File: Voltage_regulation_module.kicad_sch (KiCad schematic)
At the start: 10 parts, among them J5 PJ-202A, U6 L7805CV, U7 LD1117V33

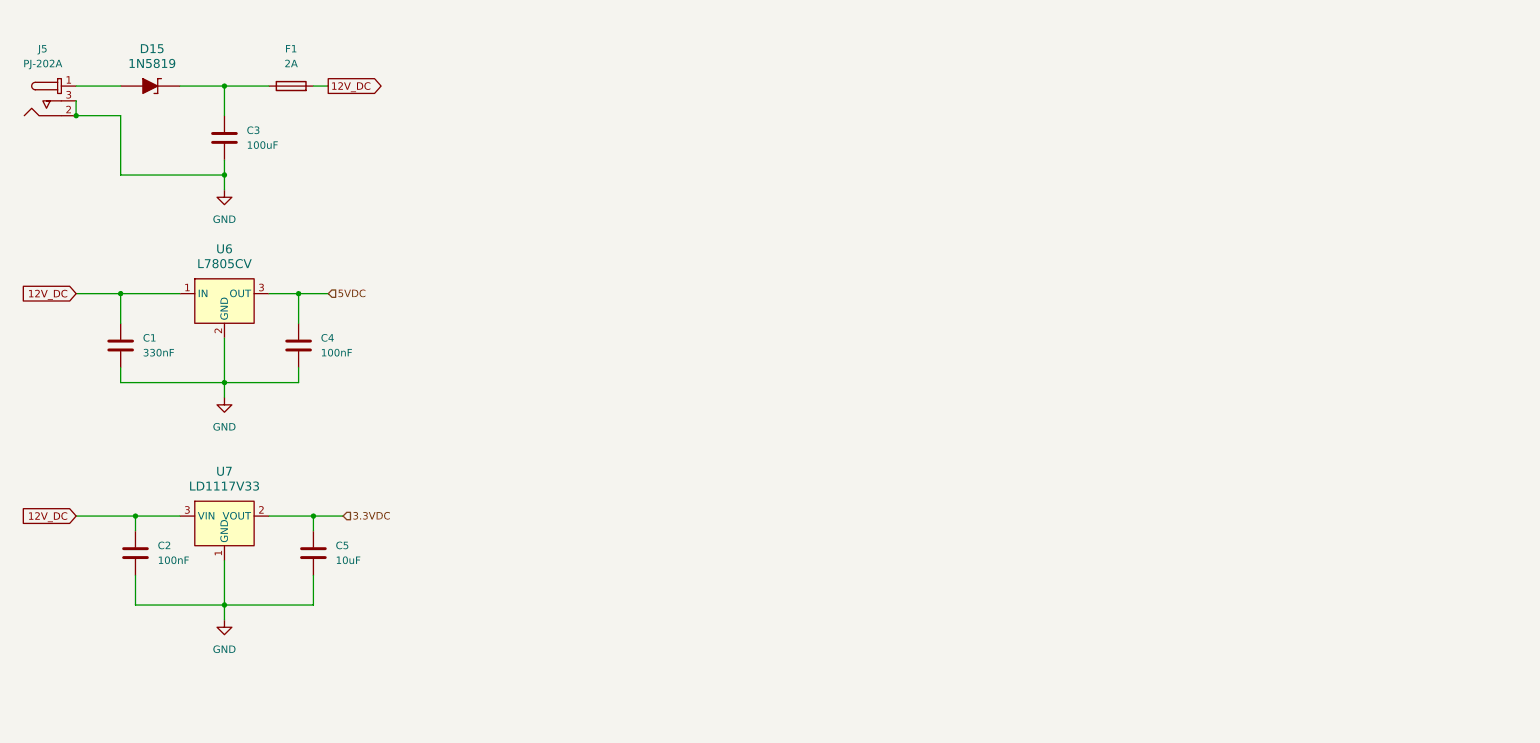
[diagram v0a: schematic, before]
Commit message: PCB REV 001 design
The design of the first revition of the PCB is complete.
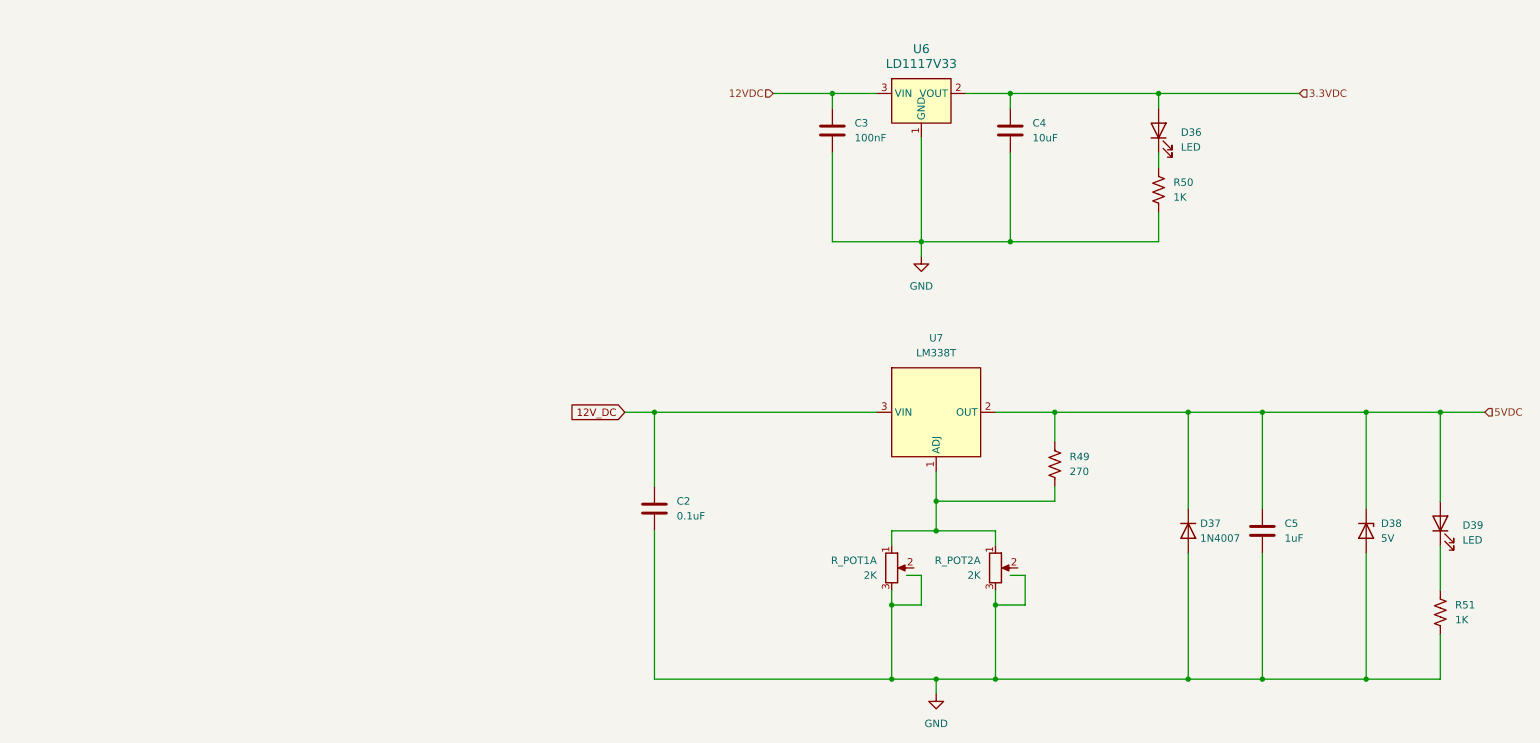
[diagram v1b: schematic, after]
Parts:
- removed C3: 100uF, Capacitor_THT:CP_Radial_D8.0mm_P5.00mm, symbol Device:C
- removed C4: 100nF, Capacitor_THT:C_Disc_D8.0mm_W5.0mm_P5.00mm, symbol Device:C
- removed D15: 1N5819, digikey-footprints:DO-41, symbol dk_Diodes-Rectifiers-Single:1N5819
- removed F1: 2A, Fuse:Fuseholder_Clip-5x20mm_Bel_FC-203-22_Lateral_P17.80x5.00mm_D1.17mm_Horizontal, symbol Device:Fuse
- removed J5: PJ-202A, digikey-footprints:Barrel_Jack_5.5mmODx2.1mmID_PJ-202A, symbol dk_Barrel-Power-Connectors:PJ-202A
- removed U6: L7805CV, digikey-footprints:TO-220-3, symbol dk_PMIC-Voltage-Regulators-Linear:L7805CV
- added C5: 1uF, Capacitor_THT:C_Radial_D10.0mm_H12.5mm_P5.00mm, symbol Device:C
- added D36, D39: LED, LED_THT:LED_D3.0mm, symbol Device:LED
- added D37: 1N4007, Diode_THT:D_DO-41_SOD81_P10.16mm_Horizontal, symbol Diode:1N4007
- added D38: 5V, Diode_THT:D_DO-35_SOD27_P10.16mm_Horizontal, symbol Device:D_Zener
- added R49: 270, Resistor_THT:R_Axial_DIN0411_L9.9mm_D3.6mm_P12.70mm_Horizontal, symbol Device:R_US
- added R50, R51: 1K, Resistor_THT:R_Axial_DIN0204_L3.6mm_D1.6mm_P5.08mm_Horizontal, symbol Device:R_US
- added R_POT1, R_POT2: 2K, Potentiometer_THT:Potentiometer_Bourns_3296W_Vertical, symbol Device:R_Potentiometer_Dual_Separate
- added U7: LM338T, Package_TO_SOT_THT:TO-220-3_Vertical, symbol MySymbols:LM338T
- C2: renamed from C1; value 330nF -> 0.1uF; footprint Capacitor_THT:C_Disc_D8.0mm_W5.0mm_P5.00mm -> Capacitor_THT:C_Radial_D10.0mm_H12.5mm_P5.00mm
- renumbered C2 to C3, C5 to C4, U7 to U6
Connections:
- net 12V_DC: now also U7.3 (VIN); no longer C3.1, U6.3 (VIN)
- net 3.3VDC: now also D36.2 (A)
- net 5VDC: now also C5.1, D37.1 (K), D38.1 (K), D39.2 (A), R49.1, U7.2 (OUT)
- net GND: now also C5.2, D37.2 (A), D38.2 (A), R50.2, R51.2, R_POT1.3, R_POT2.3
- new net: R49.2, R_POT1.1, R_POT2.1, U7.1 (ADJ)
- new net: D39.1 (K), R51.1
- new net: D36.1 (K), R50.1
- new net 12VDC: C3.1, U6.3 (VIN)
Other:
- moved on the sheet: C2, C3, C4, U6

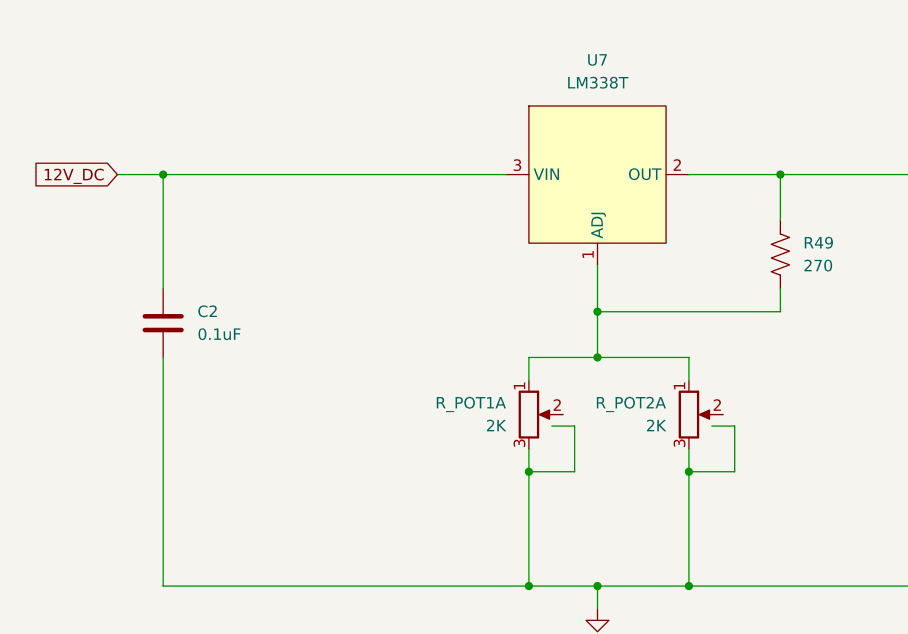
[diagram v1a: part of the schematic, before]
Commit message: PCB 90% & Corrections to diagram in the ADC section were done
Te resistors to secure a low logical level were placed, also the routing of the PCB is at the 90%
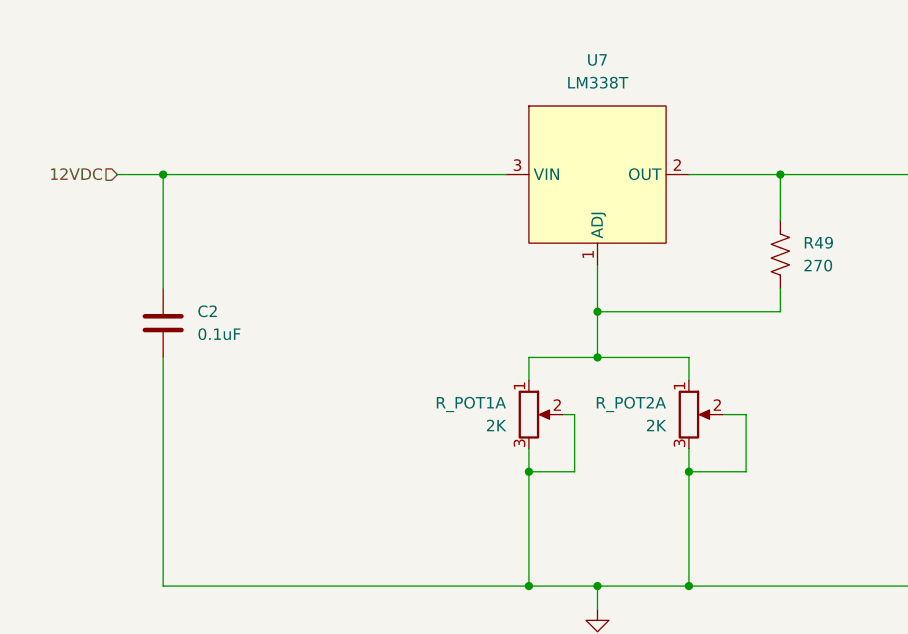
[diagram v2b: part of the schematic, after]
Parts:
- U6: footprint digikey-footprints:TO-220-3 -> Package_TO_SOT_THT:TO-220-3_Vertical
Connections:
- net 12V_DC is gone; now on net 12VDC: C2.1, U7.3 (VIN)
- net GND: now also R_POT1.2, R_POT2.2
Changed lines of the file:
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@@
 	(wire
 		(pts
-			(xy 238.76 139.7) (xy 233.68 139.7)
+			(xy 240.03 139.7) (xy 233.68 139.7)
 		)
 		(stroke
@@
 	(wire
 		(pts
-			(xy 238.76 134.62) (xy 238.76 139.7)
+			(xy 240.03 133.35) (xy 240.03 139.7)
 		)
 		(stroke
@@
 	(wire
 		(pts
-			(xy 236.22 134.62) (xy 238.76 134.62)
+			(xy 237.49 133.35) (xy 240.03 133.35)
 		)
 		(stroke
@@
 	(wire
 		(pts
-			(xy 218.44 134.62) (xy 220.98 134.62)
+			(xy 219.71 133.35) (xy 220.98 133.35)
 		)
 		(stroke
@@
 	(wire
 		(pts
-			(xy 220.98 134.62) (xy 220.98 139.7)
-		)
-		(stroke
-			(width 0)
-			(type default)
-		)
-	)
-	(global_label "12V_DC"
-		(shape input)
-		(at 170.18 106.68 180)
-		(fields_autoplaced yes)
-		(effects
-			(font
-				(size 1.27 1.27)
-			)
-			(justify right)
-		)
-		(property "Intersheetrefs" "${INTERSHEET_REFS}"
-			(at 160.1796 106.68 0)
-			(effects
-				(font
-					(size 1.27 1.27)
-				)
-				(justify right)
-				(hide yes)
-			)
+			(xy 220.98 133.35) (xy 220.98 139.7)
+		)
+		(stroke
+			(width 0)
+			(type default)
 		)
 	)
@@
 			)
 			(justify left)
+		)
+	)
+	(hierarchical_label "12VDC"
+		(shape input)
+		(at 170.18 106.68 180)
+		(fields_autoplaced yes)
+		(effects
+			(font
+				(size 1.27 1.27)
+			)
+			(justify right)
 		)
 	)
@@
 			)
 		)
-		(property "Footprint" "digikey-footprints:TO-220-3"
+		(property "Footprint" "Package_TO_SOT_THT:TO-220-3_Vertical"
 			(at 226.06 46.99 0)
 			(effects

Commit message: Backup
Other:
- note added: "encadenar al de 5v"
- note added: "np"
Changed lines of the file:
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@@
+		)
+	)
+	(text "np\n"
+		(exclude_from_sim no)
+		(at 298.704 124.46 0)
+		(effects
+			(font
+				(size 1.27 1.27)
+			)
+		)
+	)
+	(text "encadenar al de 5v\n"
+		(exclude_from_sim no)
+		(at 224.536 39.624 0)
+		(effects
+			(font
+				(size 1.27 1.27)
+			)
 		)
 	)
